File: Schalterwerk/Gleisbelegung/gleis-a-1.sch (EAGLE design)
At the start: 34 parts, among them J1 PHNX_4P_508CONN_1017493, J2 PHNX_4P_508CONN_1017493, J3 PHNX_2P_508CONN_1017491, J4 PHNX_4P_350CONN_1984989_PXC, J5 PHNX_4P_350CONN_1984989_PXC, Q1 P-MOSFET, Q2 P-MOSFET, Q3 P-MOSFET, Q4 P-MOSFET, X1 RJ45-JACK

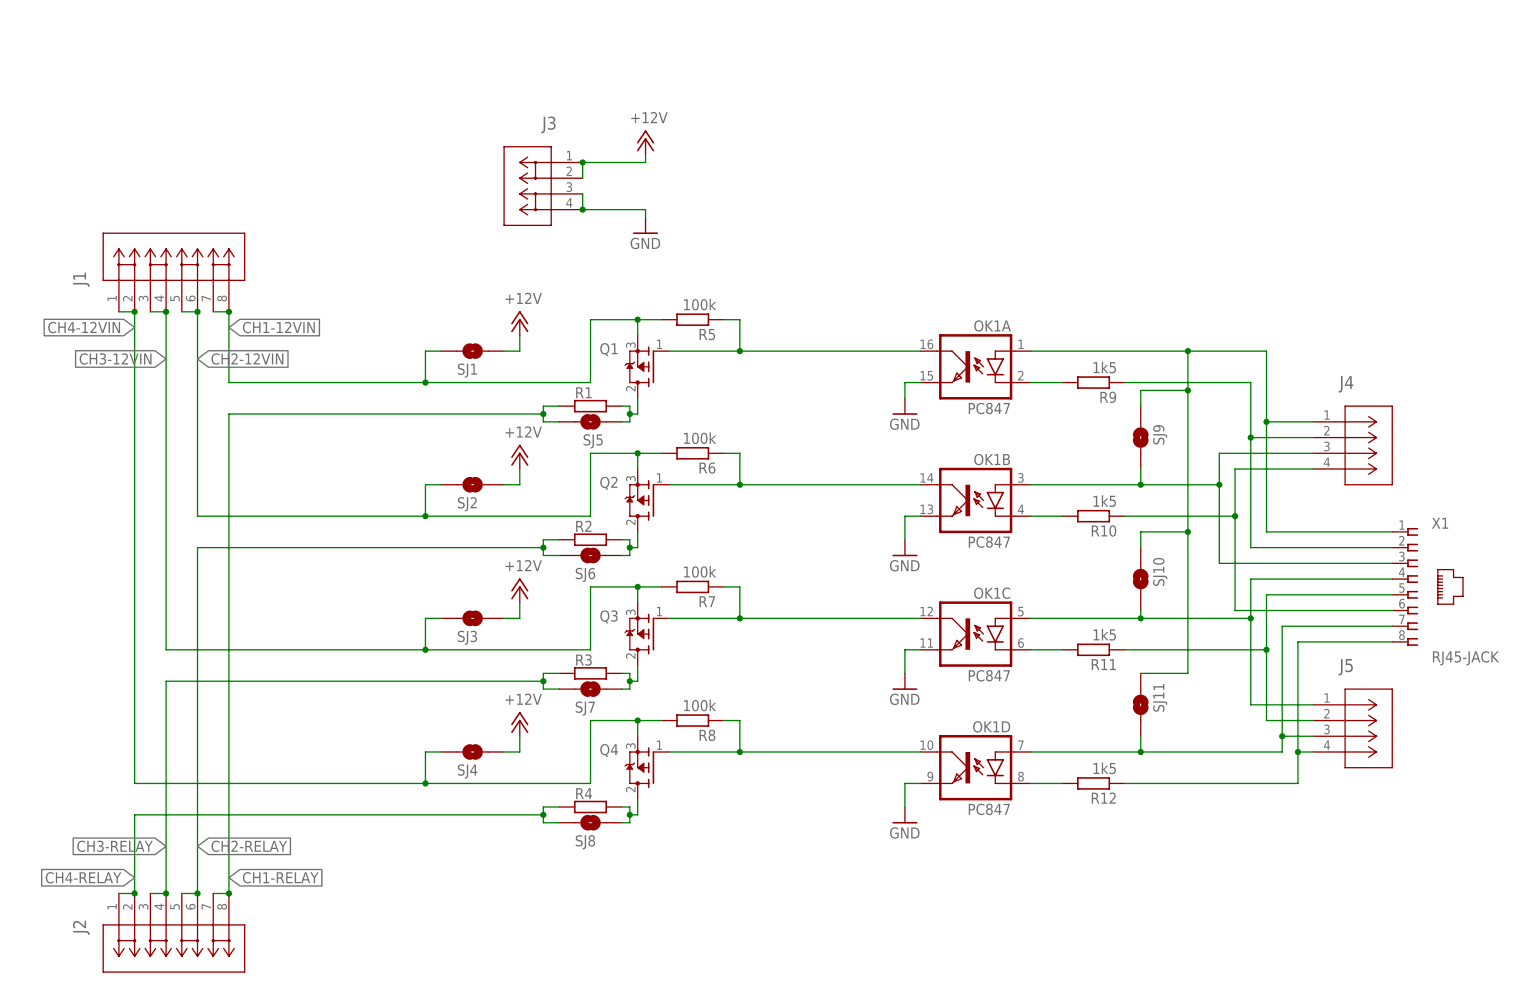
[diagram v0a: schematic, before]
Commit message: Updates the solder jumpers to connect neighboring traces on the bus side.
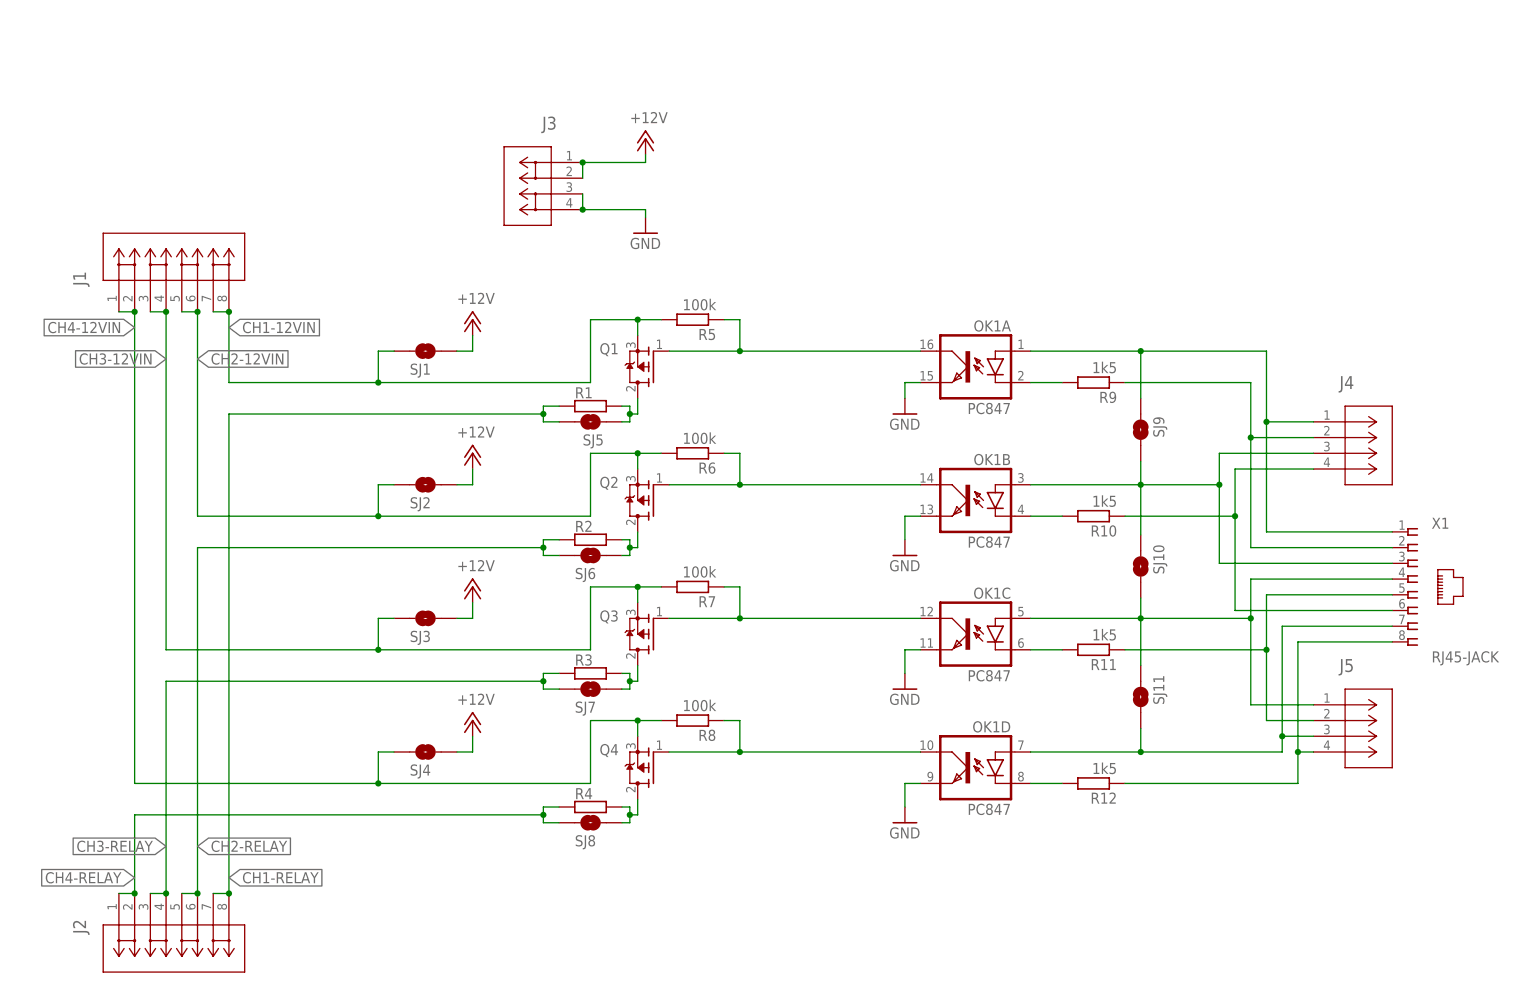
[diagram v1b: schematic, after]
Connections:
- net N$26: now also SJ11.2
- net N$3: no longer SJ10.2, SJ11.2
- net N$6: now also SJ10.2
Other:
- moved on the sheet: SJ1, SJ10, SJ11, SJ2, SJ3, SJ4, SJ9

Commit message: Updates the frames on the schematics with proper project information.
Adds LEDs for observing what is happening on the Gleisbelegtmeldung.
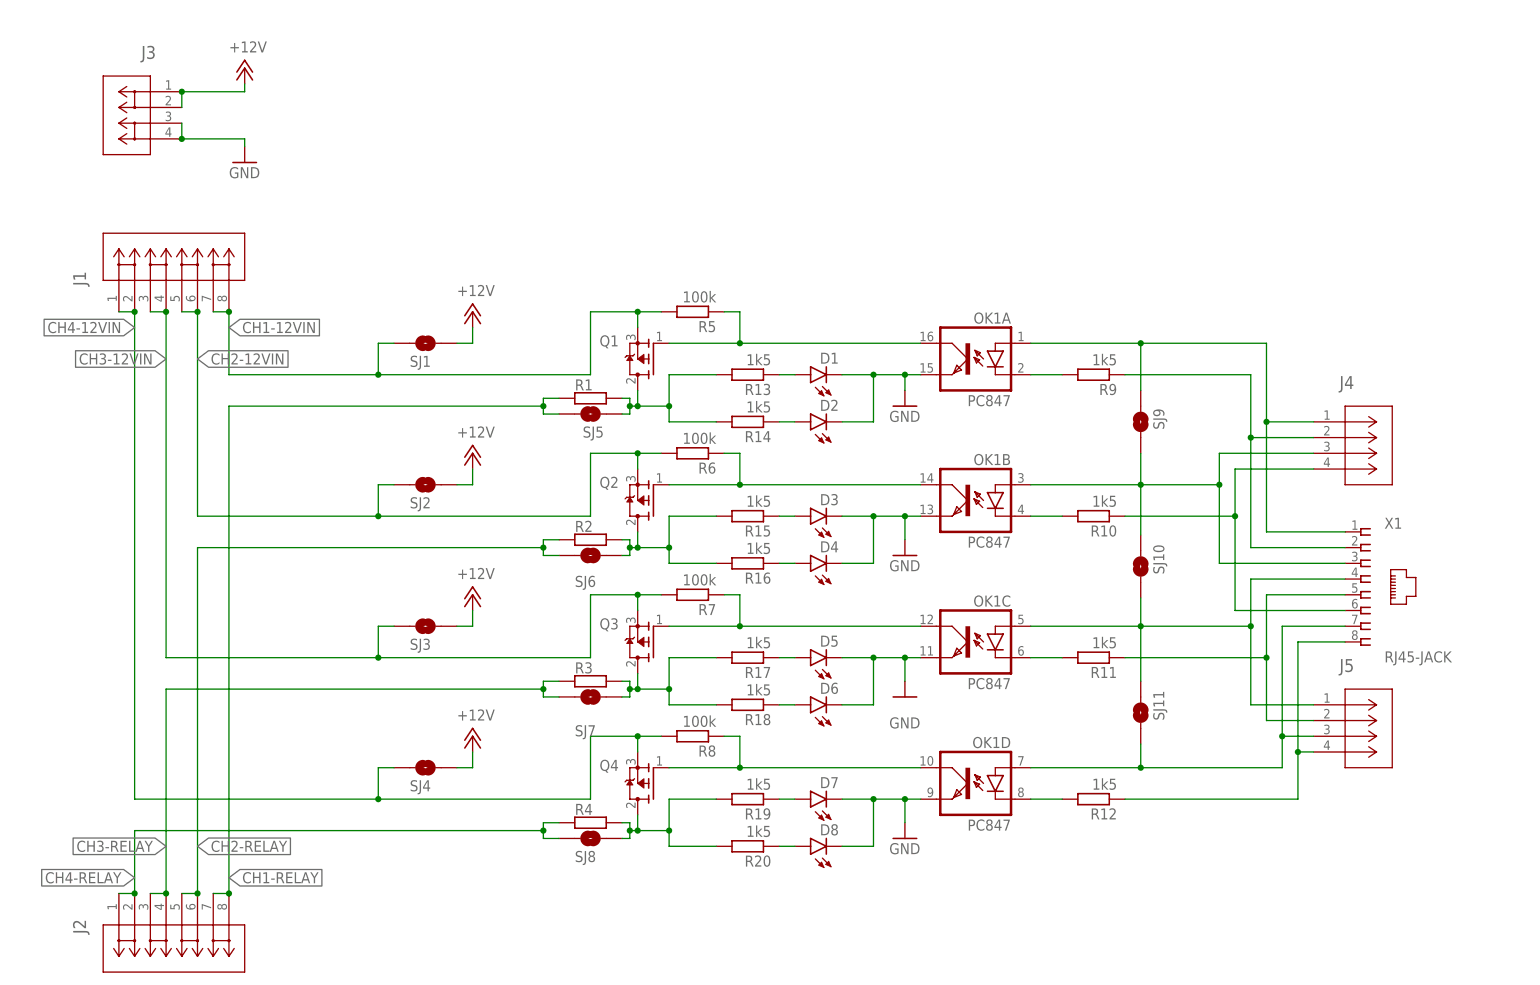
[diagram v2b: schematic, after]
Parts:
- added D1, D2, D3, D4, D5, D6, D7, D8: (no value), led:LEDCHIPLED_0603
- added R13, R14, R15, R16, R17, R18, R19, R20: 1k5, rcl:R-EU_R0805
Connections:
- new net N$21: D2.A, R14.1
- new net N$23: D3.A, R15.1
- new net N$24: D4.A, R16.1
- new net N$25: D5.A, R17.1
- new net N$27: D6.A, R18.1
- new net N$29: D7.A, R19.1
- new net N$30: D8.A, R20.1
- new net N$8: D1.A, R13.1
- net GND: now also D1.C, D2.C, D3.C, D4.C, D5.C, D6.C, D7.C, D8.C
- net N$1: now also R13.2, R14.2
- net N$10: now also R15.2, R16.2
- net N$11: now also R17.2, R18.2
- net N$13: now also R19.2, R20.2
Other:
- moved on the sheet: J3, OK1A, OK1C, OK1D, Q1, Q3, Q4, R1, R11, R12, R3, R4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

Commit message: Adds component layout to the board. Routes the isolated part of the traces.
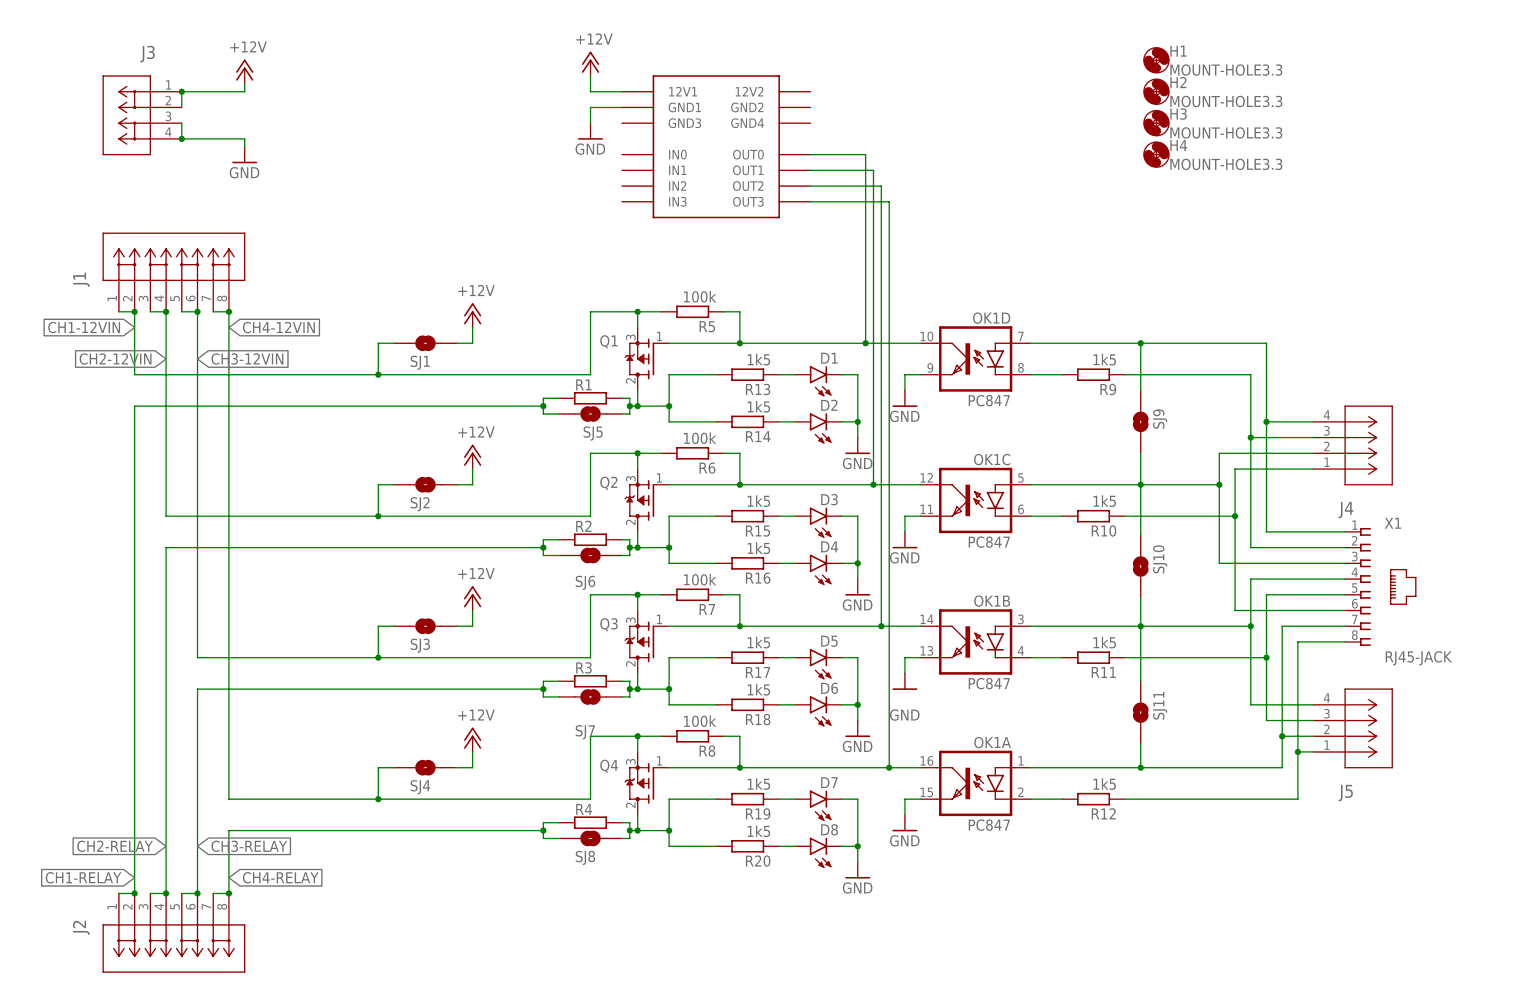
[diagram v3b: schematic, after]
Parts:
- added H1, H2, H3, H4: MOUNT-HOLE3.3, holes:MOUNT-HOLE3.3
- added X2: IO-HAT, eagleparts:IO-HAT
- D2, D4, D6, D8: value (none) -> LEDHEADER; device led:LEDCHIPLED_0603 -> eagleparts:LEDHEADER
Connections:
- net +12V: now also X2G$1.12V1
- net CH1-12VIN: now also J1.1, J1.2; no longer J1.7, J1.8
- net CH1-RELAY: now also J2.1, J2.2; no longer J2.7, J2.8
- net CH2-12VIN: now also J1.3, J1.4; no longer J1.5, J1.6
- net CH2-RELAY: now also J2.3, J2.4; no longer J2.5, J2.6
- net CH3-12VIN: now also J1.5, J1.6; no longer J1.3, J1.4
- net CH3-RELAY: now also J2.5, J2.6; no longer J2.3, J2.4
- net CH4-12VIN: now also J1.7, J1.8; no longer J1.1, J1.2
- net CH4-RELAY: now also J2.7, J2.8; no longer J2.1, J2.2
- net GND: now also X2G$1.GND1
- net N$12: now also OK1A.COL, X2G$1.OUT3; no longer OK1D.COL
- net N$14: now also J5.3; no longer J5.2
- net N$15: now also J5.2, OK1A.A; no longer J5.3, OK1D.A
- net N$16: now also J5.1; no longer J5.4
- net N$17: now also OK1D.C; no longer OK1A.C
- net N$18: now also OK1C.C; no longer OK1B.C
- net N$19: now also OK1A.C; no longer OK1D.C
- net N$2: now also OK1C.COL, X2G$1.OUT1; no longer OK1B.COL
- net N$20: now also J4.1; no longer J4.4
- net N$26: now also J5.4, OK1B.A; no longer J5.1, OK1C.A
- net N$3: now also J4.4, OK1D.A; no longer J4.1, OK1A.A
- net N$4: now also J4.3; no longer J4.2
- net N$5: now also OK1B.COL, X2G$1.OUT2; no longer OK1C.COL
- net N$6: now also J4.2, OK1C.A; no longer J4.3, OK1B.A
- net N$7: now also OK1B.C; no longer OK1C.C
- net N$9: now also OK1D.COL, X2G$1.OUT0; no longer OK1A.COL
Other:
- moved on the sheet: J4, J5, OK1A, OK1B, OK1C, OK1D

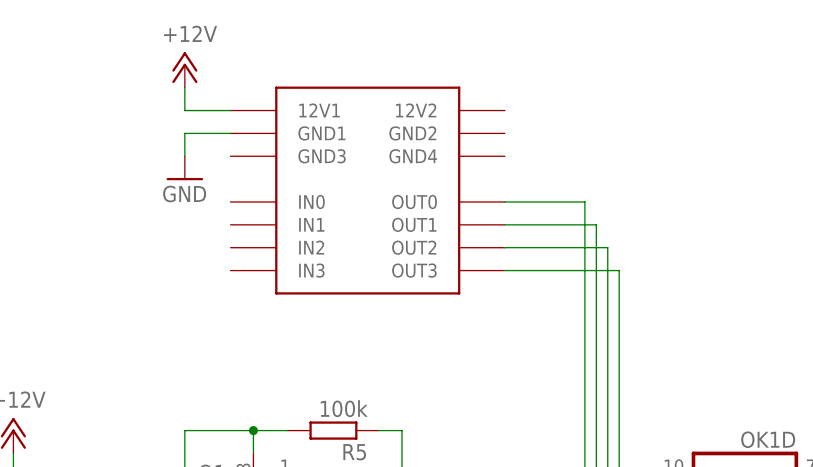
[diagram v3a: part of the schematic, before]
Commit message: Finishes routing and adds ground pour.
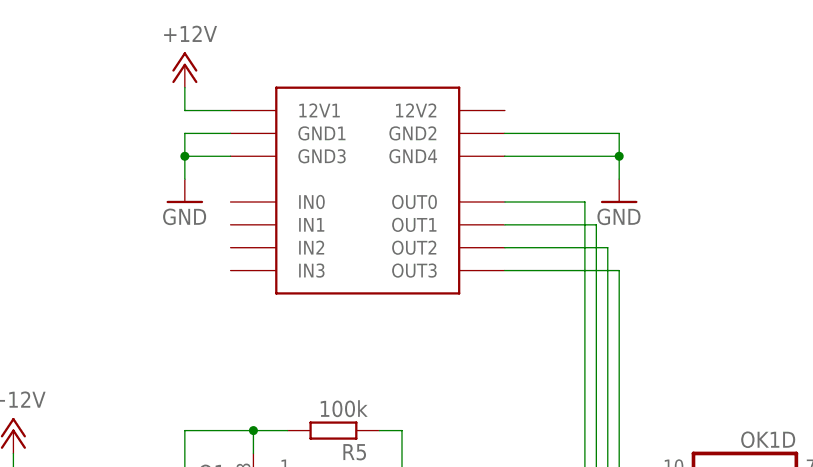
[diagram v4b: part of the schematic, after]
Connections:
- net GND: now also X2G$1.GND2, X2G$1.GND3, X2G$1.GND4
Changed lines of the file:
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@@
 <setting verticaltext="up"/>
 </settings>
-<grid distance="0.1" unitdist="inch" unit="inch" style="lines" multiple="1" display="yes" altdistance="0.05" altunitdist="inch" altunit="inch"/>
+<grid distance="0.1" unitdist="inch" unit="inch" style="lines" multiple="1" display="no" altdistance="0.01" altunitdist="inch" altunit="inch"/>
 <layers>
 <layer number="1" name="Top" color="4" fill="1" visible="no" active="no"/>
@@
 <part name="H3" library="holes" library_urn="urn:adsk.eagle:library:237" deviceset="MOUNT-HOLE" device="3.3" package3d_urn="urn:adsk.eagle:package:14278/1"/>
 <part name="H4" library="holes" library_urn="urn:adsk.eagle:library:237" deviceset="MOUNT-HOLE" device="3.3" package3d_urn="urn:adsk.eagle:package:14278/1"/>
+<part name="GND11" library="supply1" library_urn="urn:adsk.eagle:library:371" deviceset="GND" device=""/>
 </parts>
 <sheets>
@@
 <attribute name="VALUE" x="104.14" y="180.34" size="1.778" layer="96"/>
 </instance>
-<instance part="GND6" gate="1" x="106.68" y="165.1" smashed="yes">
-<attribute name="VALUE" x="104.14" y="162.56" size="1.778" layer="96"/>
+<instance part="GND6" gate="1" x="106.68" y="162.56" smashed="yes">
+<attribute name="VALUE" x="104.14" y="160.02" size="1.778" layer="96"/>
 </instance>
 <instance part="GND7" gate="1" x="149.86" y="114.3" smashed="yes">
@@
 <attribute name="NAME" x="200.152" y="163.1442" size="1.778" layer="95"/>
 <attribute name="VALUE" x="200.152" y="160.0962" size="1.778" layer="96"/>
+</instance>
+<instance part="GND11" gate="1" x="154.94" y="162.56" smashed="yes">
+<attribute name="VALUE" x="152.4" y="160.02" size="1.778" layer="96"/>
 </instance>
 </instances>
@@
 <wire x1="111.76" y1="170.18" x2="106.68" y2="170.18" width="0.1524" layer="91"/>
 <wire x1="106.68" y1="170.18" x2="106.68" y2="167.64" width="0.1524" layer="91"/>
+<pinref part="X2" gate="G$1" pin="GND3"/>
+<wire x1="106.68" y1="167.64" x2="106.68" y2="165.1" width="0.1524" layer="91"/>
+<wire x1="111.76" y1="167.64" x2="106.68" y2="167.64" width="0.1524" layer="91"/>
+<junction x="106.68" y="167.64"/>
 </segment>
 <segment>
@@
 <junction x="149.86" y="119.38"/>
 </segment>
+<segment>
+<pinref part="X2" gate="G$1" pin="GND4"/>
+<wire x1="142.24" y1="167.64" x2="154.94" y2="167.64" width="0.1524" layer="91"/>
+<pinref part="GND11" gate="1" pin="GND"/>
+<wire x1="154.94" y1="167.64" x2="154.94" y2="165.1" width="0.1524" layer="91"/>
+<pinref part="X2" gate="G$1" pin="GND2"/>
+<wire x1="142.24" y1="170.18" x2="154.94" y2="170.18" width="0.1524" layer="91"/>
+<wire x1="154.94" y1="170.18" x2="154.94" y2="167.64" width="0.1524" layer="91"/>
+<junction x="154.94" y="167.64"/>
+</segment>
 </net>

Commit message: Finalizes first version of the gleisbelegung board. Adds gerbers.
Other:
- note added: "Digitalsystem"
- note added: "Isolierung"
- note added: "Schalterwerk"
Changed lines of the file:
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@@
 <sheet>
 <plain>
+<wire x1="167.64" y1="180.34" x2="167.64" y2="33.02" width="0.1524" layer="97" style="longdash"/>
+<text x="162.56" y="182.88" size="1.778" layer="97">Isolierung</text>
+<text x="152.4" y="177.8" size="1.778" layer="97">Schalterwerk</text>
+<text x="169.418" y="177.8" size="1.778" layer="97">Digitalsystem</text>
 </plain>
 <instances>
